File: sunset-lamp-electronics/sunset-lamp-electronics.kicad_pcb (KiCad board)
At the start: 2 copper layers, 85 x 60 mm, 34 parts, among them J1 Screw_Terminal_01x02, J2 Screw_Terminal_01x02, J3 Conn_01x12_Male, J4 Conn_01x08_Male, J5 Conn_02x03_Counter_Clockwise, Q1 IRL3705N, SW1 SW_Push, U1 LM78M05CDTX/NOPB, U2 DS1307Z+T&R, U3 ATMEGA328P-AU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

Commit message: Added test LED and gitignore file
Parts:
- added D2: LED, LED_SMD:LED_0805_2012Metric_Pad1.15x1.40mm_HandSolder, F.Cu at (138.4, 75.6)
- added R8: 220R, iridium-footprints:0402-res, F.Cu at (137.8, 77.6)
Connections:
- U3 pad 12: unconnected-(U3-Pad12) -> TEST_LED
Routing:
- net TEST_LED: track 0.00 -> 15.2 mm, vias 0 -> 2
- net GND: track 31.9 -> 35.4 mm
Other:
- board text added: "LCD Contrast"
- board text added: "TEST LED"

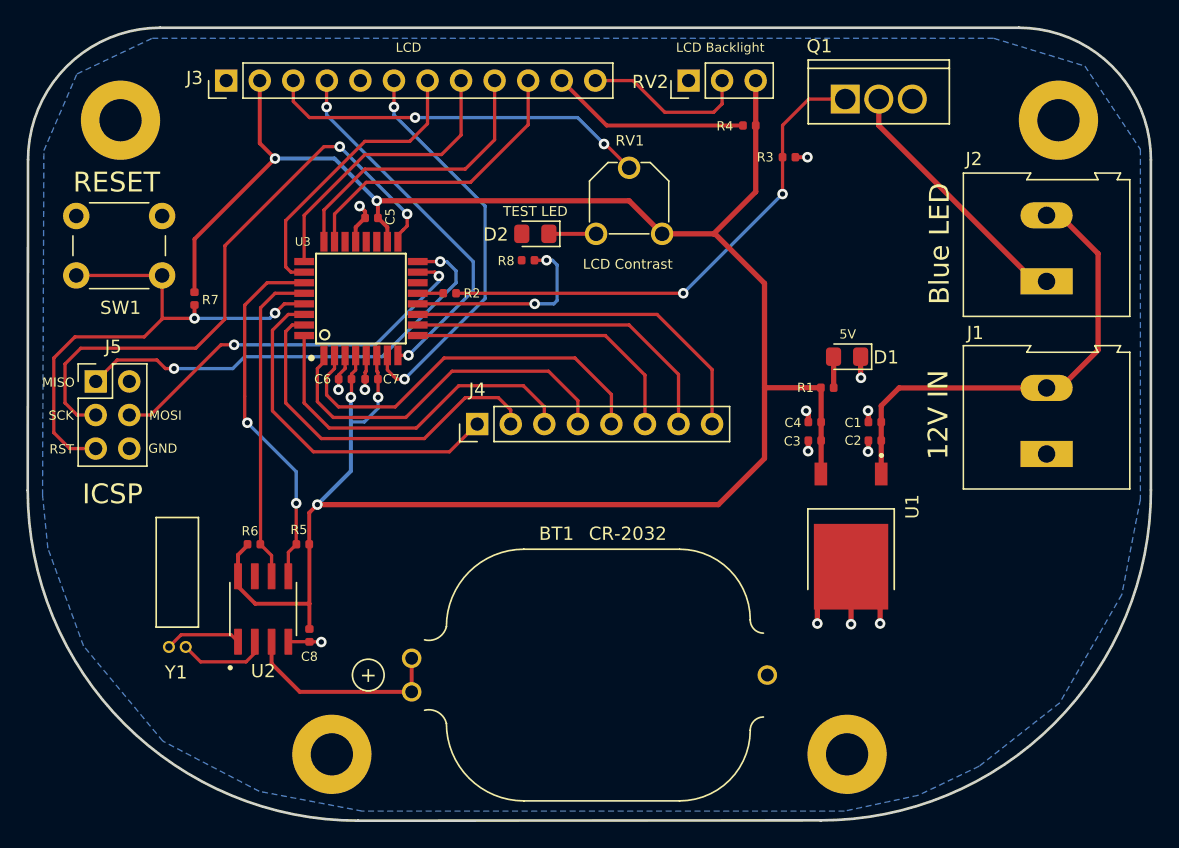
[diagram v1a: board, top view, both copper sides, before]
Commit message: Added top copper layer, vias and corrected paths
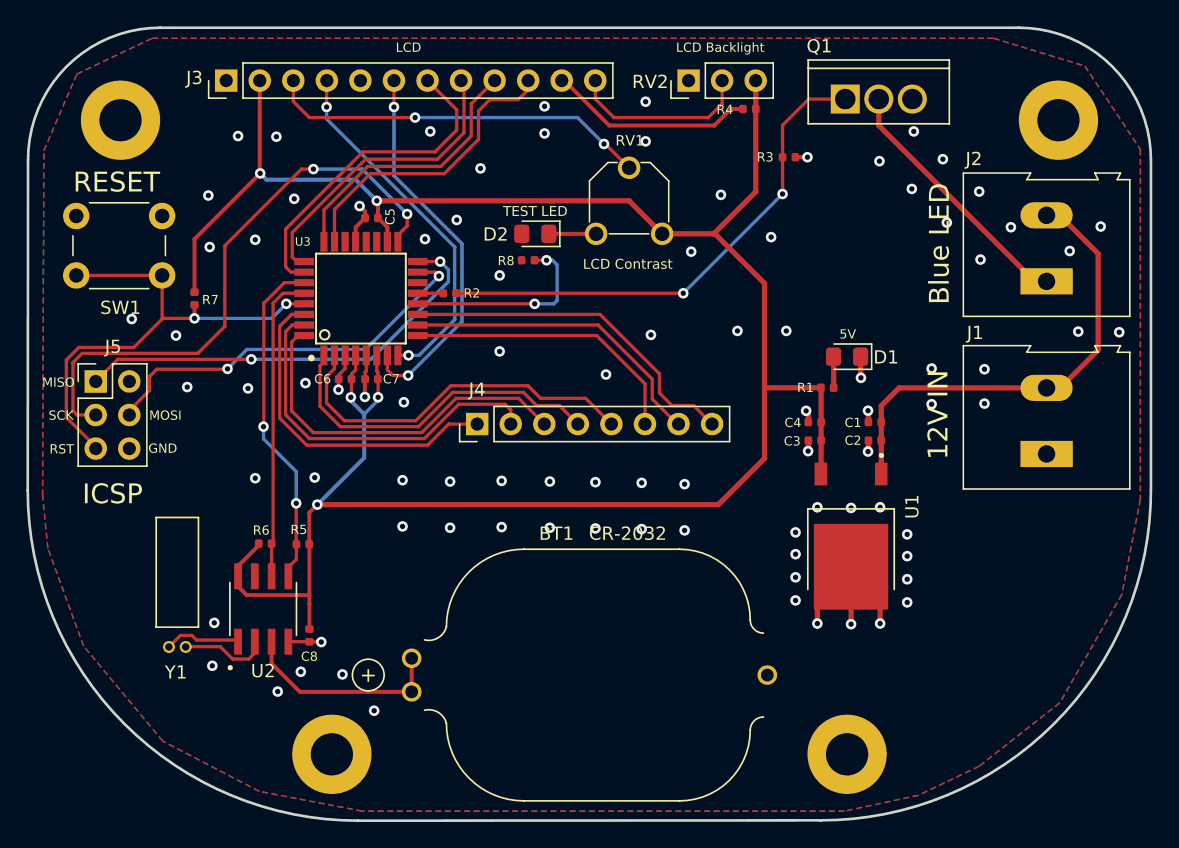
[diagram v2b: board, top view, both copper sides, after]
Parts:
- moved R4 1.25 mm to (154.6, 66.2)
- moved R6 0.85 mm to (118.0, 99.0)
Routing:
- net LCD_D4: track 22.1 -> 25.1 mm
- net ICSP_RST: track 40.8 -> 38.2 mm
- net timer_SDA: track 27.6 -> 25.7 mm
- net ICSP_SCK: track 46.1 -> 44.2 mm
- net keyboard_4: track 28.1 -> 26.2 mm
- net keyboard_5: track 30.1 -> 28.3 mm
- net ICSP_MISO: track 35.0 -> 33.3 mm
- net LCD_E: track 30.7 -> 29.0 mm
- net keyboard_8: track 28.1 -> 26.7 mm
- net keyboard_7: track 25.0 -> 23.7 mm
- net LCD_D6: track 22.0 -> 20.8 mm
- net LCD_BCKLGHT: track 12.6 -> 13.8 mm
- net timer_SCL: track 24.4 -> 23.4 mm
- net LCD_D5: track 22.0 -> 23.1 mm
- net keyboard_1: track 26.7 -> 25.6 mm
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- added copper zone on F.Cu, net GND

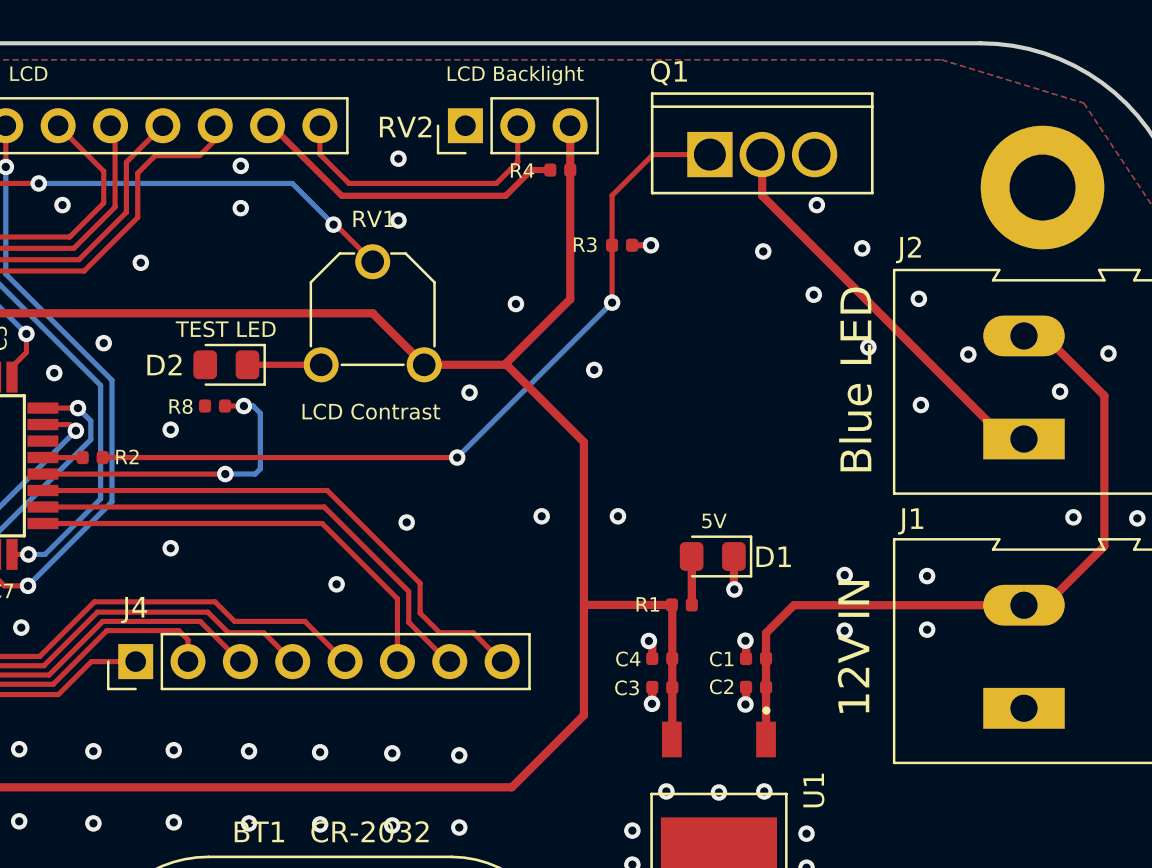
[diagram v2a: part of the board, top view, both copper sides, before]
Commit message: Updated schemat and pcb layout
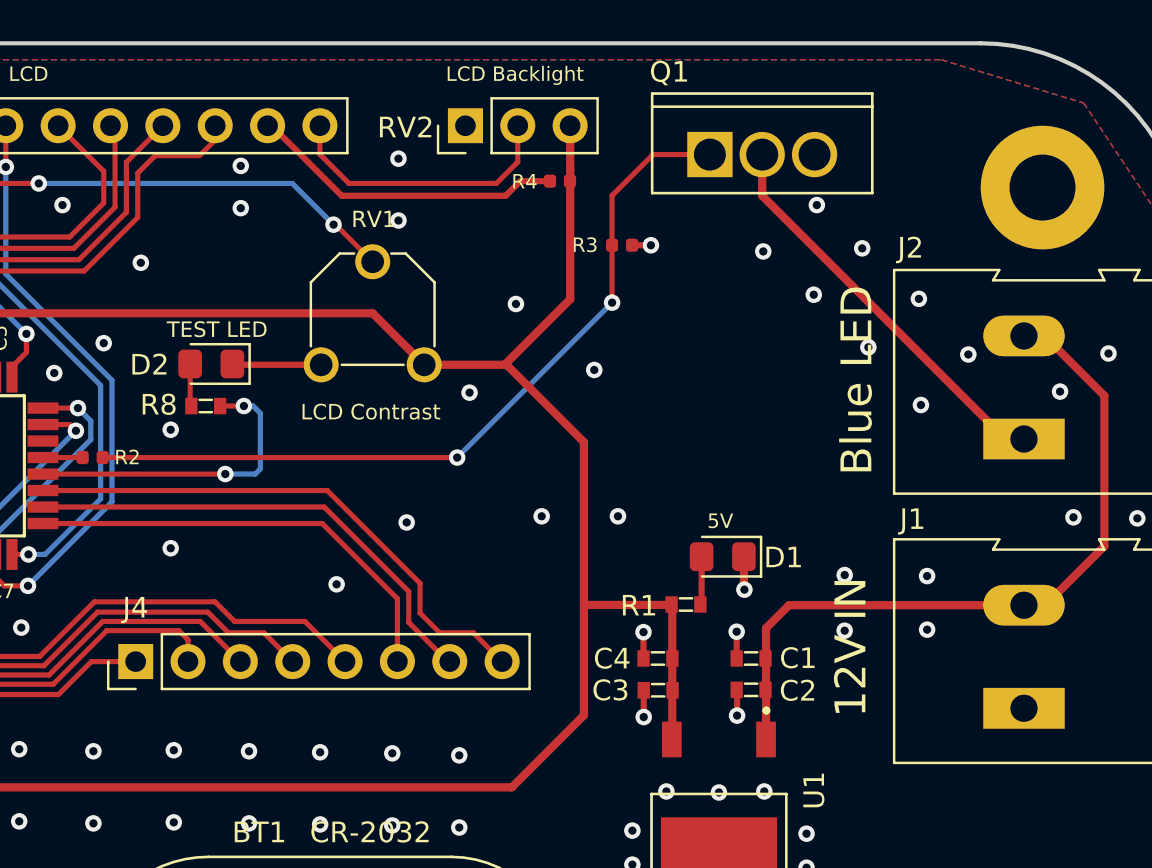
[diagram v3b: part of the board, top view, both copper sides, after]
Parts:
- C1, C2, C3, C4: footprint iridium-footprints:0402-cap -> iridium-footprints:0603-cap
- R1, R8: footprint iridium-footprints:0402-res -> iridium-footprints:0603-res
- moved D2 0.73 mm to (137.7, 75.6)
- moved R4 0.54 mm to (154.6, 66.7)
- moved D1 0.49 mm to (162.5, 84.9)
- moved R8 0.45 mm to (137.4, 77.6)
- moved C2 0.27 mm to (163.9, 91.4)
- moved C3 0.24 mm to (159.3, 91.4)
- moved C1 0.24 mm to (163.9, 89.8)
- moved C4 0.21 mm to (159.3, 89.8)
- moved R1 0.20 mm to (160.7, 87.2)
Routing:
- net GND: track 36.0 -> 38.6 mm
- net Net-(D2-Pad2): track 0.01 -> 2.06 mm
